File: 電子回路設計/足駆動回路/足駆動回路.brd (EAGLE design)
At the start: 60 x 25 mm, 22 parts, among them CN1 798-HVH-280-3P-6.5DS, IC1 TC74HC244AF, U1 BTN9990LV, U2 BTN9990LV

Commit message: 足駆動回路ヒートシンク仮設計
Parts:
- moved R6 10.2 mm to (45.3, 5.10), turned to 180 degrees
- moved R7 6.00 mm to (41.7, 4.10), turned to 180 degrees
- moved R5 6.00 mm to (41.7, 6.10), turned to 180 degrees
- moved CN2 3.00 mm to (56.0, 14.0)
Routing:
- net N$6: track 0.22 -> 11.6 mm
- net N$9: track 14.3 -> 4.49 mm
- net N$8: track 19.9 -> 10.6 mm
- net N$10: track 12.6 -> 4.50 mm
- net N$7: track 0.05 -> 4.33 mm
- net N$5: track 0.22 -> 4.37 mm
- net RPWM: track 24.1 -> 27.0 mm
- net EN: track 29.3 -> 28.0 mm, vias 2 -> 3
- net IS1: track 7.65 -> 8.89 mm
- net IS2: track 11.6 -> 12.8 mm
- net VCC: track 23.7 -> 22.9 mm
- net LPWM: track 22.3 -> 23.0 mm

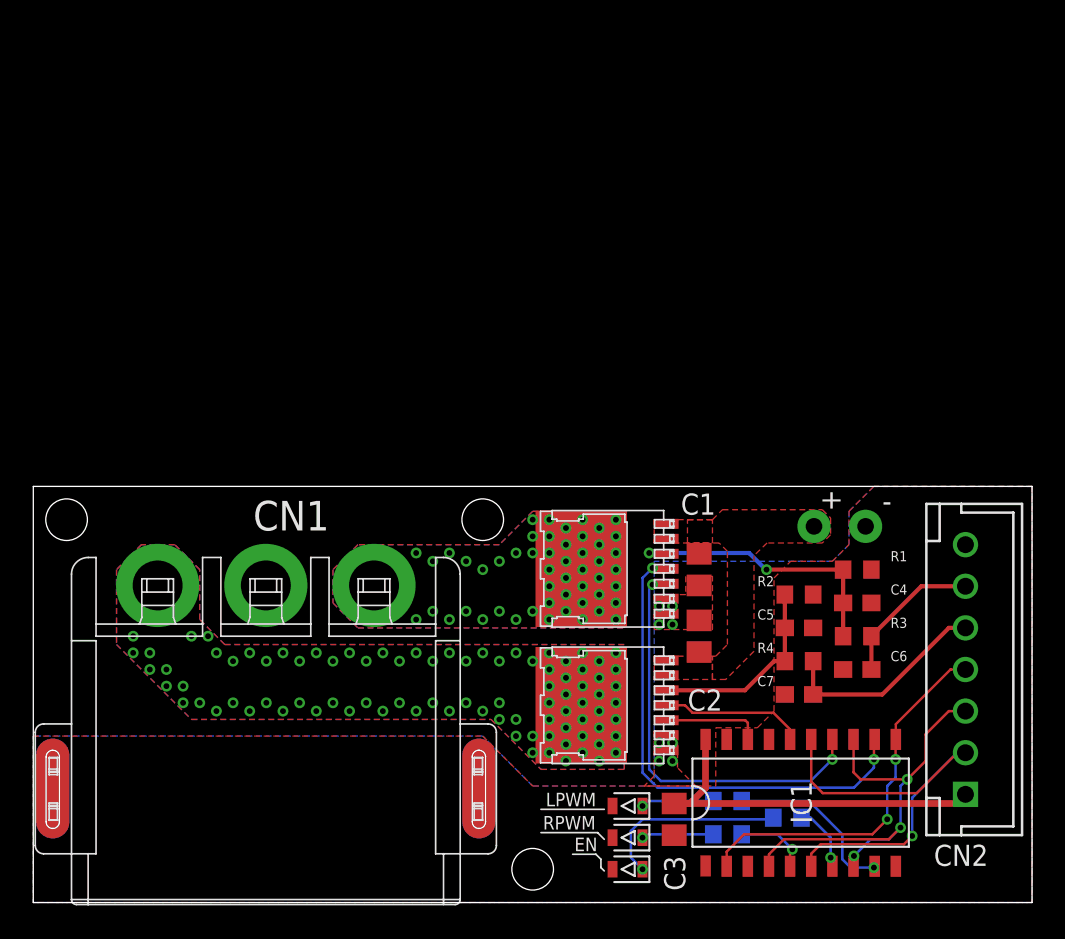
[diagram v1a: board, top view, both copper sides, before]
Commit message: ・足駆動回路設計完 ・足駆動回路ミラーバージョン作成
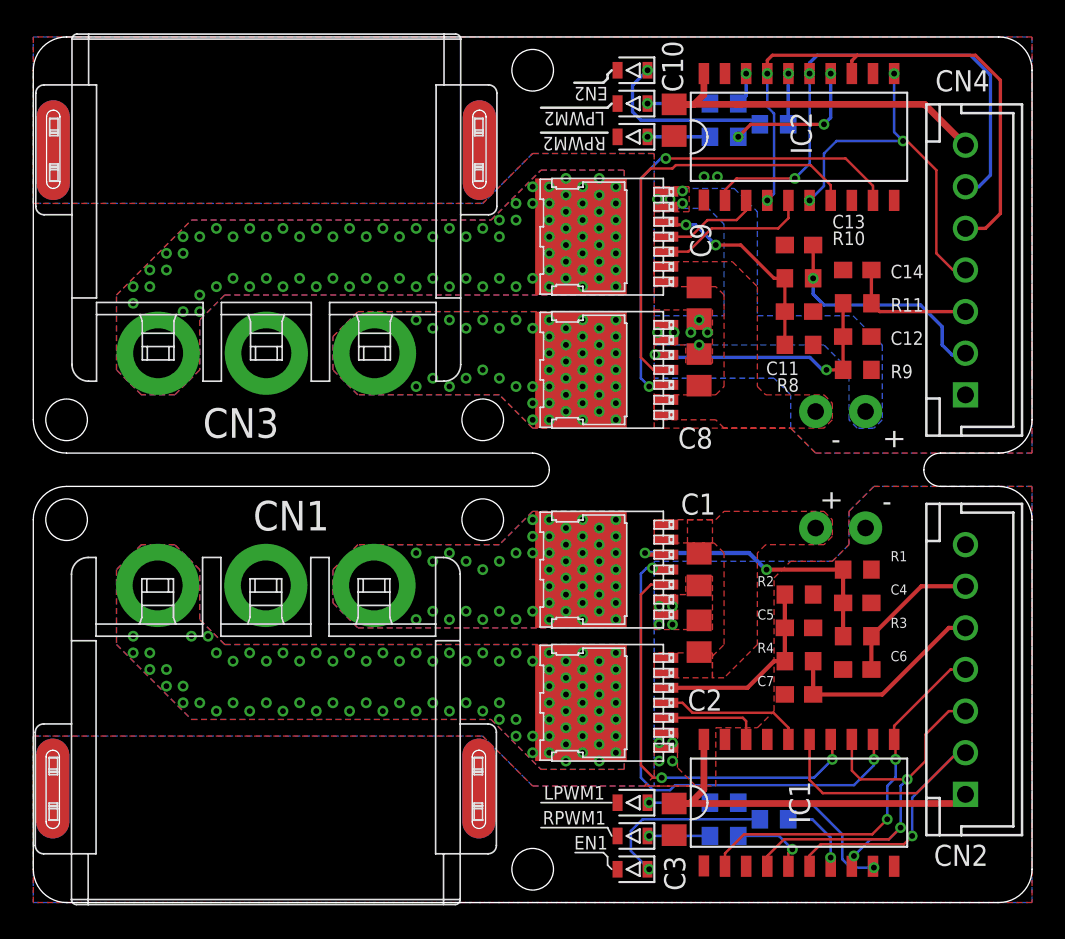
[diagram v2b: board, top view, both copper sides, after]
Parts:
- removed EN, LPWM, RPWM: OSTG1608C1A, LED:LEDC1608X39N_G
- added C10, C8, C9: 10u, RCL:C0805
- added C11, C12: 1n, RCL:C0603
- added C13, C14: 0.1u, RCL:C0603
- added CN3: 798-HVH-280-3P-6.5DS, HVH-280:798-HVH-280-3P-6.5DS
- added CN4: (no value), jst-xh:B7B-XH-A
- added EN1, EN2, LPWM1, LPWM2, RPWM1, RPWM2: OSTG1608C1A, LED:LEDC1608X39N_G
- added IC2: TC74HC244AF, 東芝_74LSシリーズ:SOP20
- added R10, R11: 150, RCL:R0603
- added R12, R13, R14: 1k, RCL:R0603
- added R8, R9: 1.5k, RCL:R0603
- added U3, U4: BTN9990LV, IT_MotorControlIC:BTN9990LV
- moved R6 0.81 mm to (44.5, 5.00)
- moved R5 0.22 mm to (41.5, 6.00)
- moved R7 0.22 mm to (41.5, 4.00)
- moved U2 0.15 mm to (34.5, 12.0)
- moved IC1 0.10 mm to (46.0, 6.00)
- moved U1 0.05 mm to (34.5, 20.0)
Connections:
- new net EN2: CN4.5, IC2.13, IC2.17, IC2.4
- new net IS12: C13.1, CN4.2, R10.1
- new net IS1_A1: C11.1, R10.2, R8.2, U3.IS
- new net IS22: C14.1, CN4.3, R11.1
- new net IS2_2: C12.1, R11.2, R9.2, U4.IS
- new net LPWM2: CN4.4, IC2.11, IC2.6
- new net N$11: IC2.9, U4.IN
- new net N$12: IC2.7, U4.INH
- new net N$13: IC2.5, U3.IN
- new net N$14: IC2.3, U3.INH
- new net N$15: R12.1, RPWM2.A
- new net N$16: EN2.A, R13.1
- new net N$17: LPWM2.A, R14.1
- new net N$18: IC2.18, R12.2
- new net N$19: IC2.16, R13.2
- new net N$20: IC2.14, R14.2
- new net OUT3: CN3.1, U3.OUT
- new net OUT4: CN3.3, U4.OUT
- new net RPWM2: CN4.6, IC2.15, IC2.2
- net GND: now also C10.2, C11.2, C12.2, C13.2, C14.2, C8.2, C9.2, CN3.P$1, CN3.P$2, CN3.P$3, CN3.P$4, CN4.1, EN1.K, EN2.K, IC2.1, IC2.10, IC2.19, LPWM1.K, LPWM2.K, R8.1, R9.1, RPWM1.K, RPWM2.K, U3.GND1, U3.GND2, U4.GND1, U4.GND2; no longer EN.K, LPWM.K, RPWM.K
- net N$5: now also LPWM1.A; no longer LPWM.A
- net N$6: now also EN1.A; no longer EN.A
- net N$7: now also RPWM1.A; no longer RPWM.A
- net VCC: now also C10.1, CN4.7, IC2.20
- net VDD: now also C8.1, C9.1, U3.VS1, U3.VS2, U4.VS1, U4.VS2
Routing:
- net EN2: track 0.00 -> 35.2 mm, vias 0 -> 2
- net RPWM2: track 0.00 -> 31.8 mm, vias 0 -> 2
- net N$11: track 0.00 -> 29.7 mm, vias 0 -> 2
- net N$12: track 0.00 -> 25.7 mm
- net LPWM2: track 0.00 -> 22.4 mm, vias 0 -> 3
- net VCC: track 22.9 -> 44.7 mm
- net IS2_2: track 0.00 -> 16.3 mm, vias 0 -> 2
- net IS12: track 0.00 -> 14.3 mm, vias 0 -> 1
- net IS1_A1: track 0.00 -> 12.6 mm, vias 0 -> 2
- net N$16: track 0.00 -> 10.8 mm, vias 0 -> 1
- net N$13: track 0.00 -> 9.26 mm
- net N$20: track 0.00 -> 8.68 mm, vias 0 -> 3
- net IS22: track 0.00 -> 7.86 mm
- net N$14: track 0.00 -> 6.08 mm
- net N$17: track 0.00 -> 3.75 mm, vias 0 -> 1
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- added copper zone on layer 1, net OUT3
- added copper zone on layer 16, net OUT3
- added copper zone on layer 1, net OUT4
- added copper zone on layer 16, net OUT4
- added copper zone on layer 16, net VDD
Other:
- board size 60 x 25 mm -> 60 x 52 mm

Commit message: fix : RMD cap
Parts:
- C1, C10, C2, C3, C8, C9: device RCL:C0805 -> 村田製作所_チップセラミックコンデンサ:C3216
- C11, C12, C13, C14, C4, C5, C6, C7: device RCL:C0603 -> 村田製作所_チップセラミックコンデンサ:C1608
- moved C8 0.90 mm to (40.0, 31.1)
- moved C1 0.70 mm to (40.0, 20.7)
- moved C2 0.40 mm to (40.0, 15.6)
- moved C9 0.20 mm to (40.0, 36.2)
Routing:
- net VCC: track 44.7 -> 46.4 mm

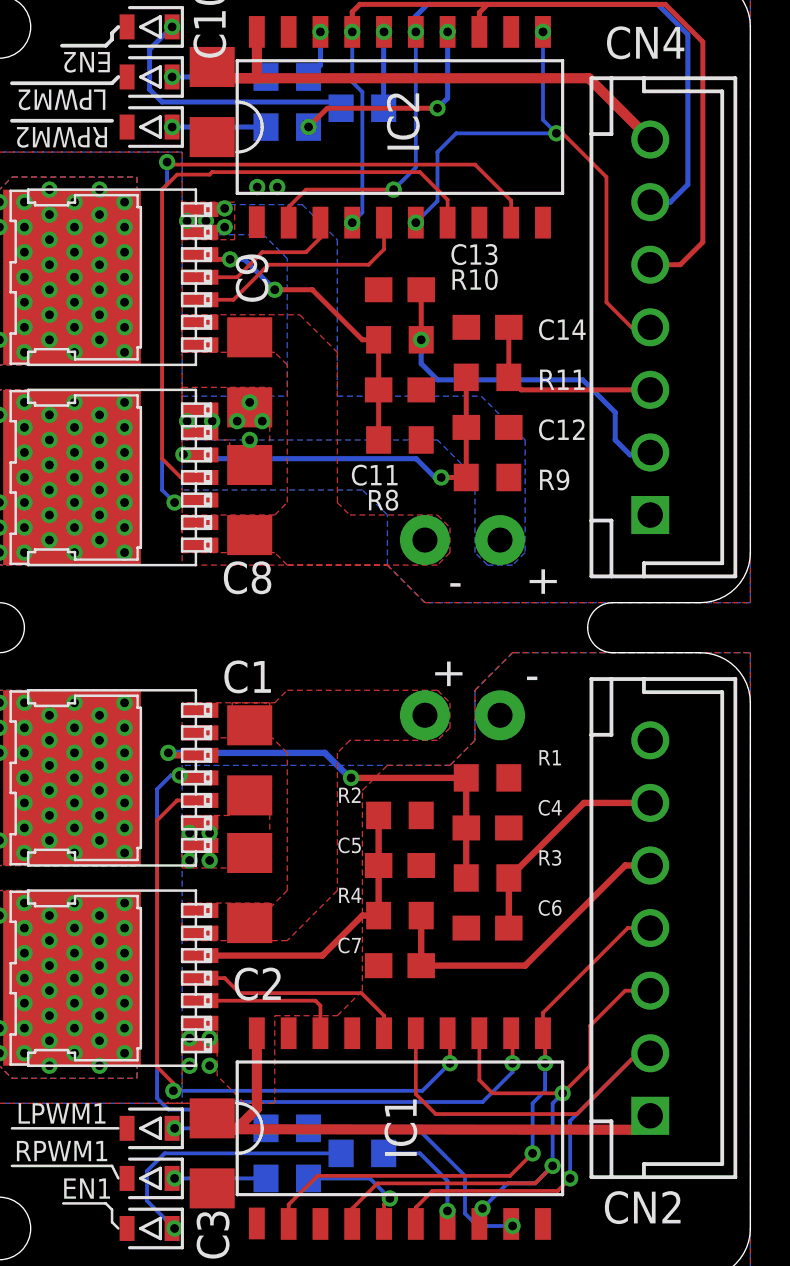
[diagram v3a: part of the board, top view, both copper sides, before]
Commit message: fix : RMD res / add : RMD cam
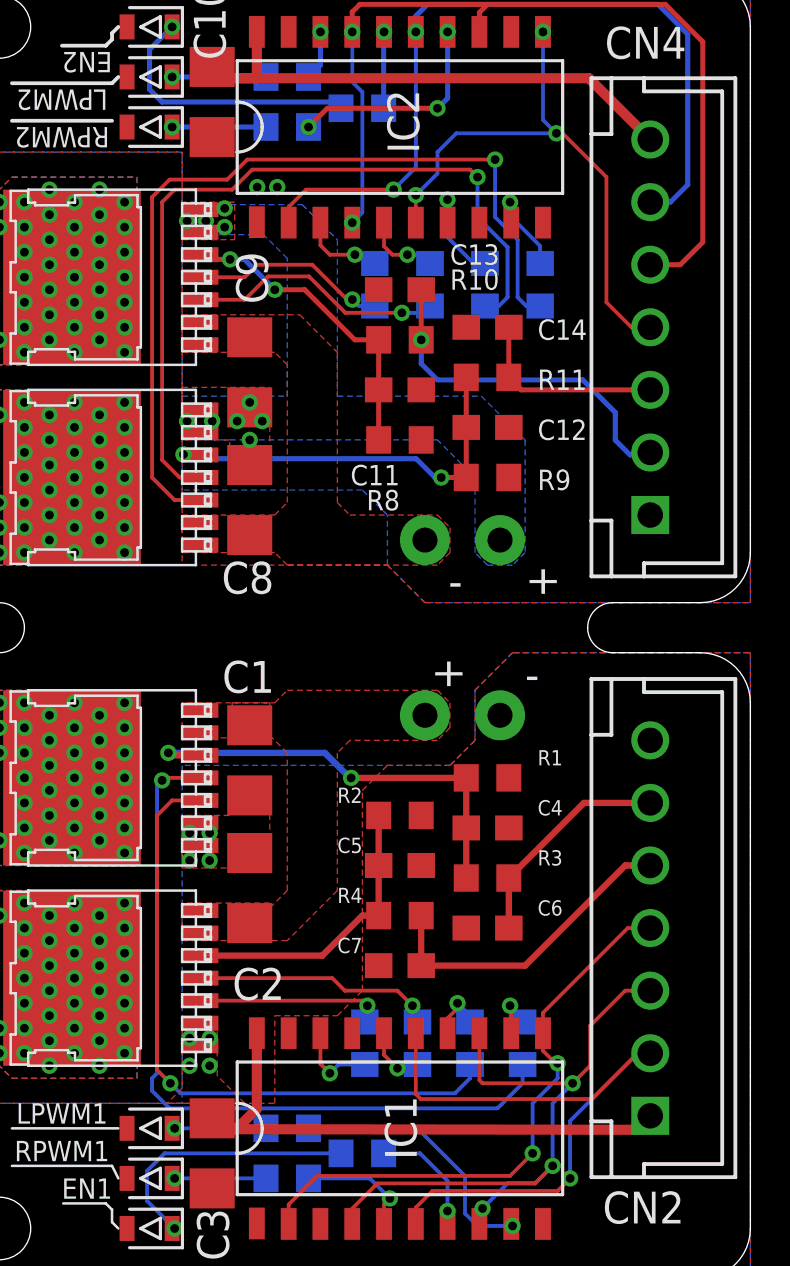
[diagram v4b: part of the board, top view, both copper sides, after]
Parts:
- added R15, R16, R17, R18, R19, R20, R21, R22: 10k, FLE_抵抗器:R1608
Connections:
- new net N$21: R15.2, U1.INH
- new net N$22: R16.2, U1.IN
- new net N$23: R17.2, U2.INH
- new net N$24: R18.2, U2.IN
- new net N$25: R19.2, U3.IN
- new net N$26: R20.2, U3.INH
- new net N$27: R21.2, U4.IN
- new net N$28: R22.2, U4.INH
- net N$1: now also R18.1; no longer U2.IN
- net N$11: now also R21.1; no longer U4.IN
- net N$12: now also R22.1; no longer U4.INH
- net N$13: now also R19.1; no longer U3.IN
- net N$14: now also R20.1; no longer U3.INH
- net N$2: now also R17.1; no longer U2.INH
- net N$3: now also R16.1; no longer U1.IN
- net N$4: now also R15.1; no longer U1.INH
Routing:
- net N$27: track 0.00 -> 34.7 mm, vias 0 -> 1
- net N$28: track 0.00 -> 31.7 mm, vias 0 -> 1
- net N$21: track 0.00 -> 30.4 mm, vias 0 -> 1
- net N$4: track 30.9 -> 2.05 mm, vias 2 -> 1
- net N$11: track 30.2 -> 3.79 mm, vias 2 -> 1
- net N$22: track 0.00 -> 25.8 mm, vias 0 -> 1
- net N$3: track 25.8 -> 2.32 mm, vias 2 -> 1
- net N$12: track 25.6 -> 4.36 mm, vias 0 -> 1
- net N$25: track 0.00 -> 10.3 mm, vias 0 -> 1
- net N$23: track 0.00 -> 9.69 mm, vias 0 -> 1
- net N$26: track 0.00 -> 7.89 mm, vias 0 -> 1
- net N$24: track 0.00 -> 7.47 mm, vias 0 -> 1
- net N$2: track 8.69 -> 2.48 mm, vias 0 -> 1
- net N$13: track 9.26 -> 3.06 mm, vias 0 -> 1
- net N$1: track 6.01 -> 3.30 mm, vias 0 -> 1
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
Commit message: fix : cam data
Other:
- board text added: "C1"
- board text added: "C10"
- board text added: "C11"
- board text added: "C12"
- board text added: "C13"
- board text added: "C14"
- board text added: "C2"
- board text added: "C3"
- board text added: "C4"
- board text added: "C5"
- board text added: "C6"
- board text added: "C7"
- board text added: "C8"
- board text added: "C9"
- board text added: "CN1"
- board text added: "CN2"
- board text added: "CN3"
- board text added: "CN4"
- board text added: "EN1"
- board text added: "EN2"
- board text added: "IC1"
- board text added: "IC2"
- board text added: "LPWM1"
- board text added: "LPWM2"
- board text added: "R1"
- board text added: "R10"
- board text added: "R11"
- board text added: "R12"
- board text added: "R13"
- board text added: "R14"
- board text added: "R15"
- board text added: "R16"
- board text added: "R17"
- board text added: "R18"
- board text added: "R19"
- board text added: "R2"
- board text added: "R20"
- board text added: "R21"
- board text added: "R22"
- board text added: "R3"
- board text added: "R4"
- board text added: "R5"
- board text added: "R6"
- board text added: "R7"
- board text added: "R8"
- board text added: "R9"
- board text added: "RPWM1"
- board text added: "RPWM2"
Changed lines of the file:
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@@
 <drawing>
 <settings>
-<setting alwaysvectorfont="yes"/>
+<setting alwaysvectorfont="no"/>
 <setting verticaltext="up"/>
 </settings>
@@
 <layer number="97" name="Info" color="7" fill="1" visible="no" active="no"/>
 <layer number="98" name="Guide" color="6" fill="1" visible="no" active="no"/>
+<layer number="121" name="_tPlace" color="14" fill="1" visible="yes" active="yes"/>
+<layer number="125" name="_tNames" color="14" fill="1" visible="yes" active="yes"/>
+<layer number="126" name="_bNames" color="5" fill="1" visible="yes" active="yes"/>
 </layers>
 <board>
-<fusionsync huburn="a.YnVzaW5lc3M6MTFiaWdzdG9uZTE" projecturn="a.YnVzaW5lc3M6MTFiaWdzdG9uZTEjMjAyMzA0MTQ2MzA0MzgwMzE" f3durn="urn:adsk.wipprod:dm.lineage:Bg-MxRAbSdOYoYSgc2-JMA" pcbguid="144be031-0638-435b-a34c-0f17c5d598f9" lastpulledtime="" lastsyncedchangeguid="" latestrevisionid="451f3918-48fa-4799-bfe6-95b5e16cd4b3" lastsyncedrevisionid="451f3918-48fa-4799-bfe6-95b5e16cd4b3" lastboardhashguid="0ff0fcd1-aa0d-571a-64ff-7686d0eaa3f4" lastpushedtime="2023-07-12T04:37:25Z" linktopcb3d="true"/>
+<fusionsync huburn="a.YnVzaW5lc3M6MTFiaWdzdG9uZTE" projecturn="a.YnVzaW5lc3M6MTFiaWdzdG9uZTEjMjAyMzA0MTQ2MzA0MzgwMzE" f3durn="urn:adsk.wipprod:dm.lineage:Bg-MxRAbSdOYoYSgc2-JMA" pcbguid="" lastpulledtime="" lastsyncedchangeguid="" latestrevisionid="451f3918-48fa-4799-bfe6-95b5e16cd4b3" lastsyncedrevisionid="451f3918-48fa-4799-bfe6-95b5e16cd4b3" lastboardhashguid="0ff0fcd1-aa0d-571a-64ff-7686d0eaa3f4" lastpushedtime="2023-07-12T04:37:25Z" linktopcb3d="true"/>
 <plain>
 <polygon width="0.15" layer="29">
@@
 <text x="48.5" y="28.5" size="1.27" layer="21" rot="R180">-</text>
 <text x="51" y="28.5" size="1.27" layer="21" rot="R270">+</text>
+<text x="38.899996875" y="23.400003125" size="1.27" layer="125">C1</text>
+<text x="41.39999375" y="12.4" size="1.27" layer="125" rot="R180">C2</text>
+<text x="37.9" y="2.79999375" size="1.27" layer="125" rot="R270">C3</text>
+<text x="51.5" y="18.4999875" size="0.6096" layer="125">C4</text>
+<text x="43.499990625" y="16.999990625" size="0.6096" layer="125">C5</text>
+<text x="51.5" y="14.499996875" size="0.6096" layer="125">C6</text>
+<text x="43.499990625" y="13" size="0.6096" layer="125">C7</text>
+<text x="40.969996875" y="28.629990625" size="1.27" layer="125" rot="R180">C8</text>
+<text x="40.72999375" y="38.929996875" size="1.27" layer="125" rot="R90">C9</text>
+<text x="37.770003125" y="51.77" size="1.27" layer="125" rot="R270">C10</text>
+<text x="46.000009375" y="32.5000125" size="0.8128" layer="125" rot="R180">C11</text>
+<text x="51.5" y="33.500009375" size="0.8128" layer="125">C12</text>
+<text x="48.00000625" y="40.49999375" size="0.8128" layer="125">C13</text>
+<text x="51.5" y="37.5" size="0.8128" layer="125">C14</text>
+<text x="17.78" y="24.13" size="1.778" layer="125" rot="R180">CN1</text>
+<text x="54.09999375" y="2.199996875" size="1.27" layer="125" ratio="10">CN2</text>
+<text x="10.189996875" y="27.920009375" size="1.778" layer="125">CN3</text>
+<text x="57.45" y="50.000003125" size="1.27" layer="125" ratio="10" rot="R180">CN4</text>
+<text x="33.500009375" y="3.999990625" size="0.8128" layer="125" rot="R180" align="bottom-center">EN1</text>
+<text x="33.500009375" y="49.000003125" size="0.8128" layer="125" rot="SR180" align="bottom-center">EN2</text>
+<text x="45.400009375" y="7.300009375" size="1.27" layer="121" rot="R270">IC1</text>
+<text x="45.500009375" y="47.50000625" size="1.27" layer="121" rot="R270">IC2</text>
+<text x="32.5000125" y="7.0000125" size="0.8128" layer="125" rot="R180" align="bottom-center">LPWM1</text>
+<text x="32.5000125" y="47.50000625" size="0.8128" layer="125" rot="SR180" align="bottom-center">LPWM2</text>
+<text x="51.5" y="20.500009375" size="0.6096" layer="125">R1</text>
+<text x="43.499990625" y="18.9999875" size="0.6096" layer="125">R2</text>
+<text x="51.5" y="16.49999375" size="0.6096" layer="125">R3</text>
+<text x="43.499990625" y="14.999996875" size="0.6096" layer="125">R4</text>
+<text x="37.565" y="6.4650125" size="1.27" layer="126" rot="MR180">R5</text>
+<text x="46.165009375" y="5.7650125" size="1.27" layer="126" rot="MR180">R6</text>
+<text x="37.665" y="4.664990625" size="1.27" layer="126" rot="MR180">R7</text>
+<text x="46.000009375" y="31.4999875" size="0.8128" layer="125" rot="R180">R8</text>
+<text x="51.5" y="31.4999875" size="0.8128" layer="125">R9</text>
+<text x="48.00000625" y="39.499996875" size="0.8128" layer="125">R10</text>
+<text x="51.5" y="35.50000625" size="0.8128" layer="125">R11</text>
+<text x="39.86499375" y="50.365" size="1.27" layer="126" rot="MR180">R12</text>
+<text x="46.36500625" y="47.61499375" size="1.27" layer="126" rot="MR180">R13</text>
+<text x="39.86499375" y="44.865009375" size="1.27" layer="126" rot="MR180">R14</text>
+<text x="50.2" y="9.40000625" size="0.8128" layer="126" rot="MR270" align="bottom-center">R15</text>
+<text x="48.10000625" y="9.40000625" size="0.8128" layer="126" rot="MR270" align="bottom-center">R16</text>
+<text x="46.000009375" y="9.40000625" size="0.8128" layer="126" rot="MR270" align="bottom-center">R17</text>
+<text x="44.6000125" y="7.800009375" size="0.8128" layer="126" rot="MR180" align="bottom-center">R18</text>
+<text x="46.500009375" y="39.699996875" size="0.8128" layer="126" rot="MR270" align="bottom-center">R19</text>
+<text x="44.2999875" y="39.699996875" size="0.8128" layer="126" rot="MR270" align="bottom-center">R20</text>
+<text x="50.9" y="39.699996875" size="0.8128" layer="126" rot="MR270" align="bottom-center">R21</text>
+<text x="48.700003125" y="39.699996875" size="0.8128" layer="126" rot="MR270" align="bottom-center">R22</text>
+<text x="32.5000125" y="5.4999875" size="0.8128" layer="125" rot="R180" align="bottom-center">RPWM1</text>
+<text x="32.5000125" y="46.000009375" size="0.8128" layer="125" rot="SR180" align="bottom-center">RPWM2</text>
 </plain>
 <attributes>
